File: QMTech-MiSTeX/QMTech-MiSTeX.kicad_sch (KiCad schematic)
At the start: 42 parts, among them J1 RPi_GPIO, J12 Conn_01x03_Pin, J13 USB_C_Receptacle_USB2.0, J2 MiSTer SDRAM Module, J3 USB_C_Receptacle_USB2.0, J4 Conn_02x32_Odd_Even, J5 Conn_02x32_Odd_Even, J6 Conn_01x06_Pin, J7 Conn_01x03_Pin, J8 Conn_01x03_Pin

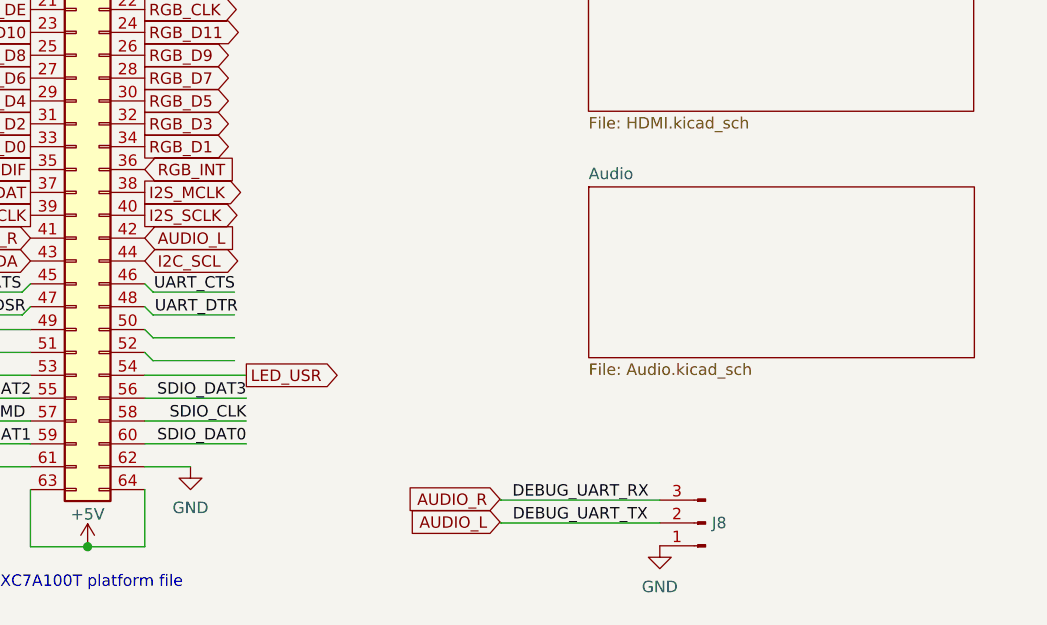
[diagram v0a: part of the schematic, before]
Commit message: connect two remaining pins to new 2 row Pmod, fix via, tidy test points
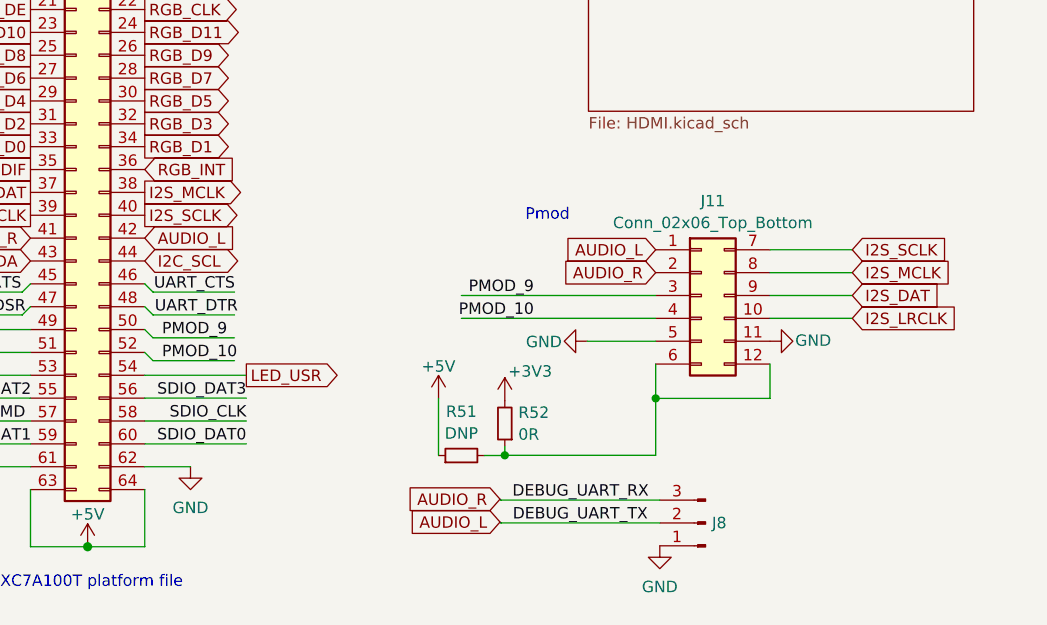
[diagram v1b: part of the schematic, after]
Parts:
- added J11: Conn_02x06_Top_Bottom, Connector_PinSocket_2.54mm:PinSocket_2x06_P2.54mm_Horizontal, symbol Connector_Generic:Conn_02x06_Top_Bottom
- added R51: DNP, R_0603_1608Metric, symbol jlcpcb-basic-resistor-0603:0R
- added R52: 0R, R_0603_1608Metric, symbol jlcpcb-basic-resistor-0603:0R
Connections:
- net +3V3: now also R52.2
- net +5V: now also R51.1
- net AUDIO_L: now also J11.1 (Pin_1)
- net AUDIO_R: now also J11.2 (Pin_2)
- net GND: now also J11.11 (Pin_11), J11.5 (Pin_5)
- net I2S_DAT: now also J11.9 (Pin_9)
- net I2S_LRCLK: now also J11.10 (Pin_10)
- net I2S_MCLK: now also J11.8 (Pin_8)
- net I2S_SCLK: now also J11.7 (Pin_7)
- net PMOD_9: now reaches J5.50 (Pin_50)
- net PMOD_9: now also J11.3 (Pin_3)
- net PMOD_10: now reaches J5.52 (Pin_52)
- net PMOD_10: now also J11.4 (Pin_4)
- new net: J11.12 (Pin_12), J11.6 (Pin_6), R51.2, R52.1
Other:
- removed sheet Audio
- note added: "Pmod"

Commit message: don't include DNP parts in BOM
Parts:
- R51: LCSC C21189 -> (none)
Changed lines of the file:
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@@
-      (effects (font (size 1.27 1.27)) hide)
-    )
-    (property "LCSC" "C21189" (at 217.17 93.98 90)
       (effects (font (size 1.27 1.27)) hide)
     )

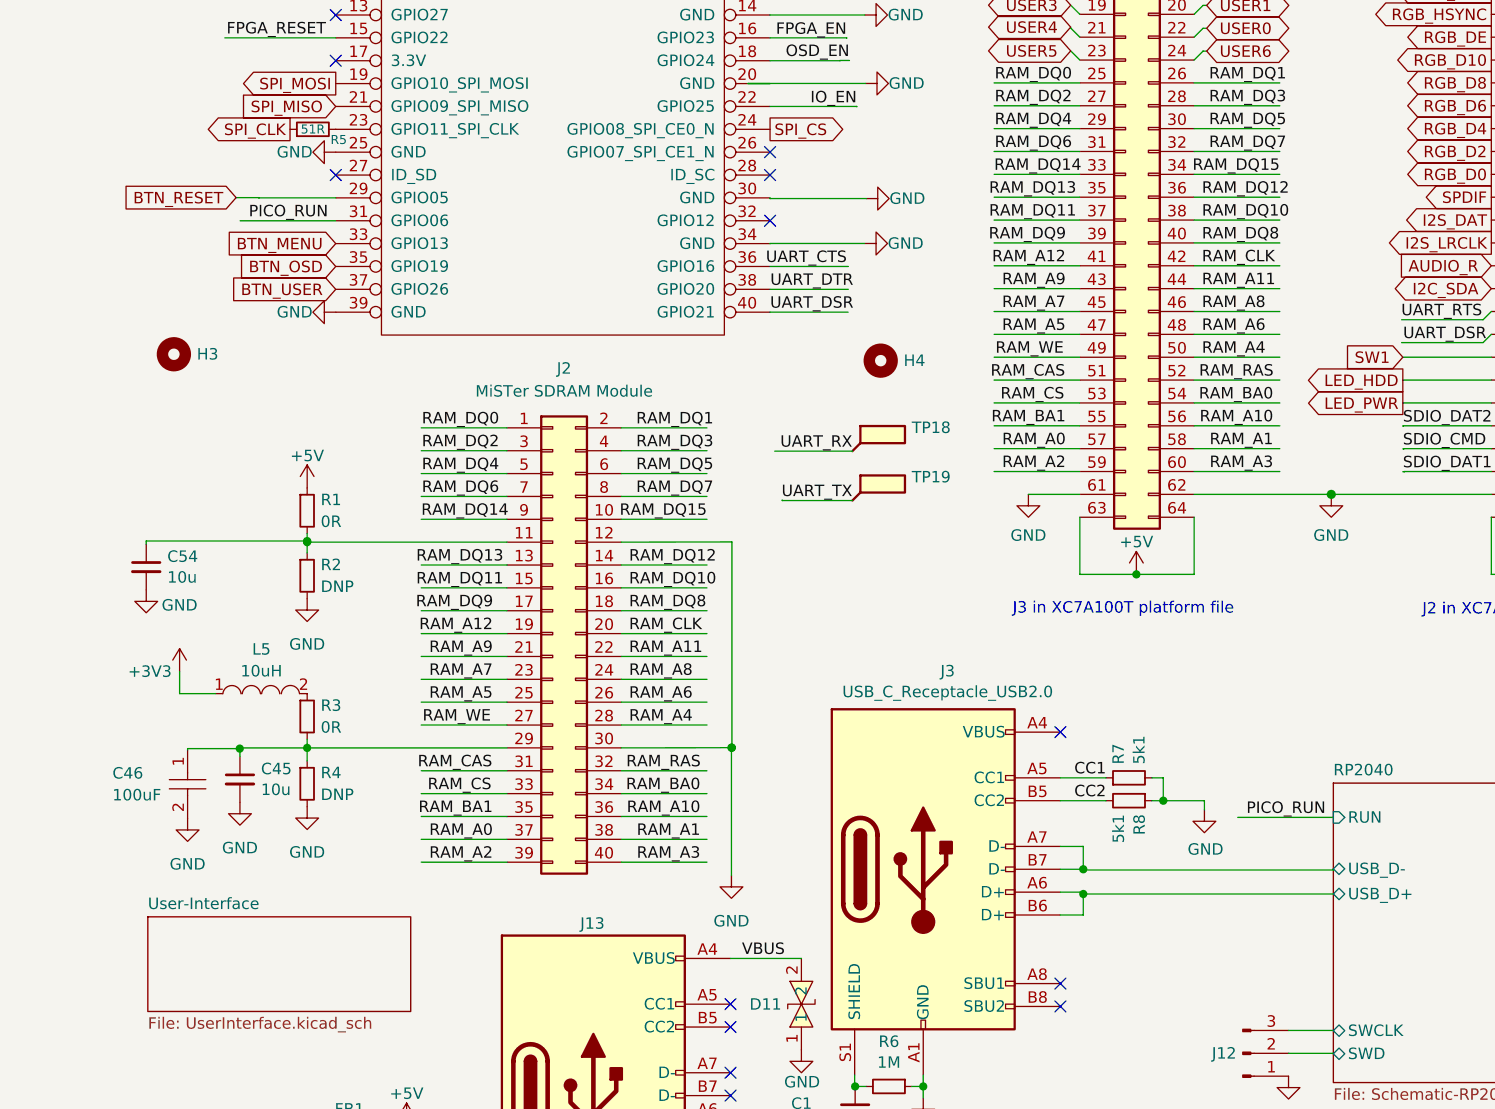
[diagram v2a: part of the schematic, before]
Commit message: add front switch, reroute USB, test points
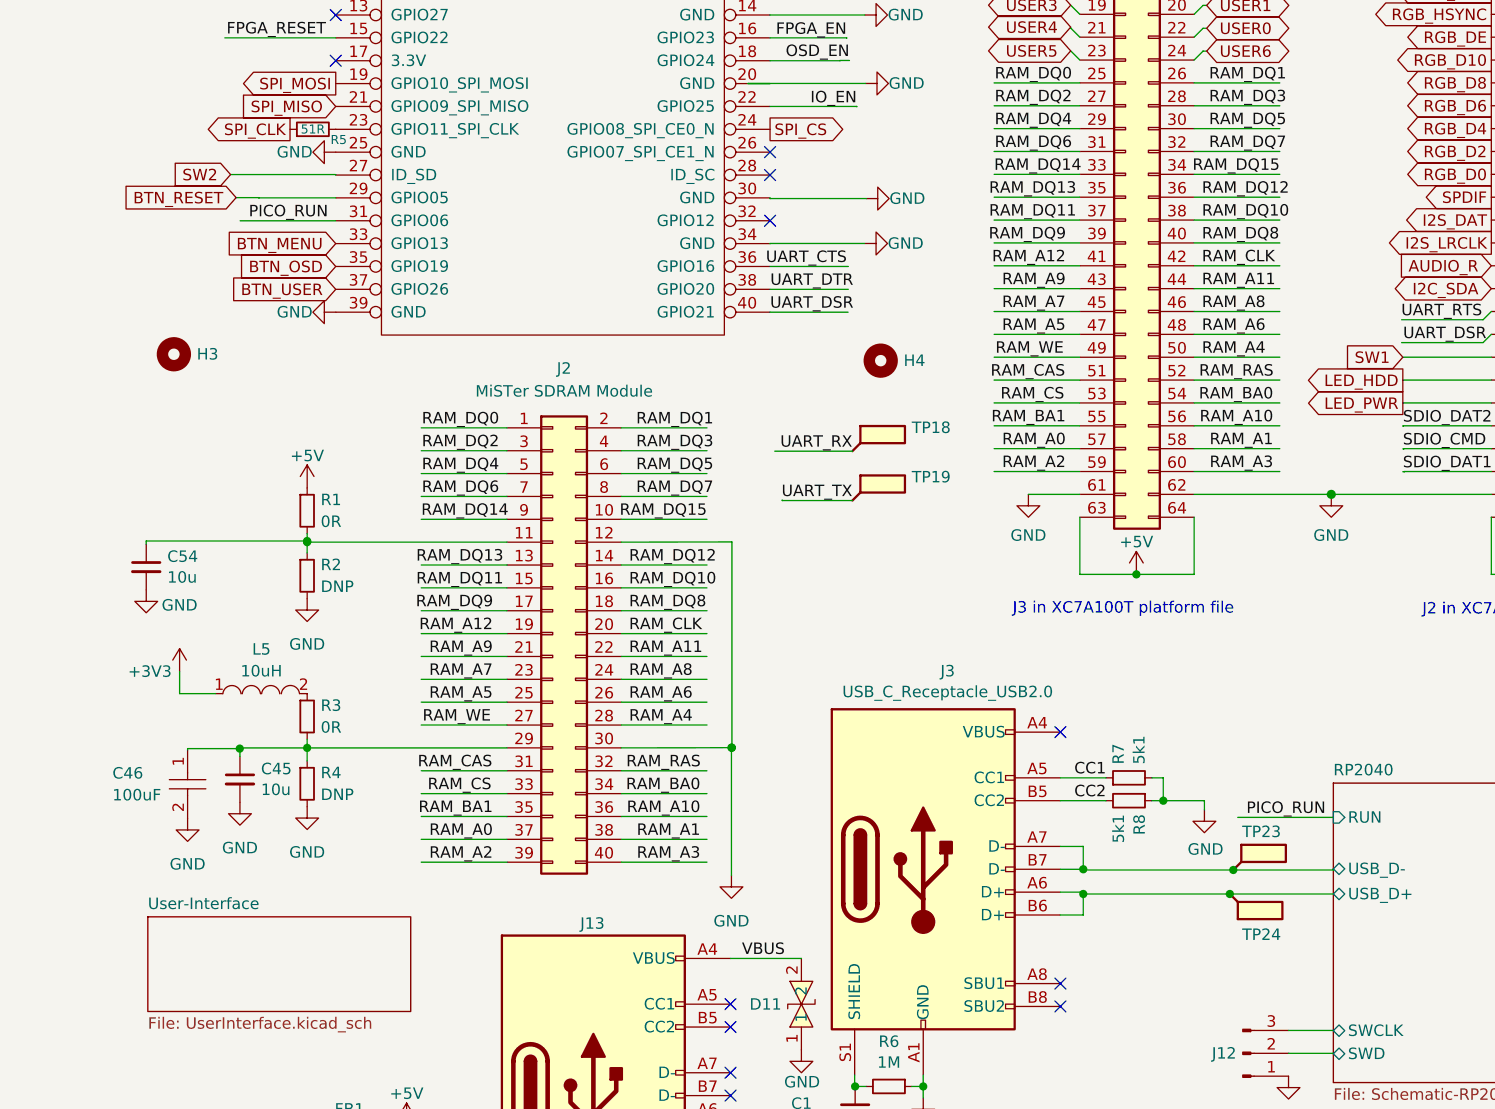
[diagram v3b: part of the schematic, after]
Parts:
- added TP23, TP24: TestPoint_Flag, TestPoint:TestPoint_Pad_D1.5mm, symbol Connector:TestPoint_Flag
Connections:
- net RP2040/USB_D+: now also TP24.1
- net RP2040/USB_D-: now also TP23.1
- net SW2: now reaches J1.27 (ID_SD)
- no-connect marks 20 -> 19
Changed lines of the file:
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@@
   (junction (at 84.9122 123.3678) (diameter 0) (color 0 0 0 0)
   )
+  (junction (at 140.2377 139.6238) (diameter 0) (color 0 0 0 0)
+  )
   (junction (at 175.641 104.1146) (diameter 1.016) (color 0 0 0 0)
   )
@@
   (junction (at 123.952 139.6238) (diameter 0) (color 0 0 0 0)
   )
+  (junction (at 140.6214 136.9568) (diameter 0) (color 0 0 0 0)
+  )
   (junction (at 238.76 87.63) (diameter 0) (color 0 0 0 0)
   )
@@
   (no_connect (at 40.894 26.7208))
   (no_connect (at 84.7598 177.2666))
-  (no_connect (at 40.894 59.7408))
   (no_connect (at 89.154 64.8208))
   (no_connect (at 89.154 59.7408))
@@
     (stroke (width 0) (type default))
   )
+  (wire (pts (xy 29.21 59.69) (xy 40.894 59.69))
+    (stroke (width 0) (type default))
+  )
   (wire (pts (xy 245.364 151.765) (xy 228.2952 151.765))
     (stroke (width 0) (type default))
@@
     (stroke (width 0) (type default))
   )
+  (wire (pts (xy 40.894 59.69) (xy 40.894 59.7408))
+    (stroke (width 0) (type default))
+  )
   (wire (pts (xy 182.9054 80.899) (xy 181.991 79.9846))
     (stroke (width 0) (type default))
@@
     (stroke (width 0) (type default))
   )
+  (wire (pts (xy 140.6214 136.9568) (xy 151.7396 136.9568))
+    (stroke (width 0) (type default))
+  )
   (wire (pts (xy 181.991 97.7646) (xy 181.991 104.1146))
     (stroke (width 0) (type solid))
@@
     (stroke (width 0) (type default))
   )
+  (wire (pts (xy 140.2377 139.6238) (xy 151.7396 139.6238))
+    (stroke (width 0) (type default))
+  )
   (wire (pts (xy 151.7142 154.7876) (xy 151.7396 154.813))
     (stroke (width 0) (type default))
@@
     (stroke (width 0) (type default))
   )
-  (wire (pts (xy 123.952 139.6238) (xy 151.7396 139.6238))
+  (wire (pts (xy 123.952 139.6238) (xy 140.2377 139.6238))
     (stroke (width 0) (type default))
   )
@@
     (stroke (width 0) (type default))
   )
-  (wire (pts (xy 123.952 136.9568) (xy 151.7396 136.9568))
+  (wire (pts (xy 123.952 136.9568) (xy 140.6214 136.9568))
     (stroke (width 0) (type default))
   )
@@
     )
   )
+  (global_label "SW2" (shape input) (at 29.21 59.69 180) (fields_autoplaced)
+    (effects (font (size 1.27 1.27)) (justify right))
+    (property "Intersheetrefs" "${INTERSHEET_REFS}" (at 22.2593 59.69 0)
+      (effects (font (size 1.27 1.27)) (justify right))
+    )
+  )
   (global_label "RGB_D12" (shape output) (at 169.291 39.3446 180) (fields_autoplaced)
     (effects (font (size 1.27 1.27)) (justify right))
@@
     )
   )
+  (symbol (lib_id "Connector:TestPoint_Flag") (at 140.2377 139.6238 0) (mirror x) (unit 1)
+    (in_bom yes) (on_board yes) (dnp no)
+    (property "Reference" "TP24" (at 141.605 144.145 0)
+      (effects (font (size 1.27 1.27)) (justify left))
+    )
+    (property "Value" "TestPoint_Flag" (at 146.8417 139.8087 0)
+      (effects (font (size 1.27 1.27)) (justify left) hide)
+    )
+    (property "Footprint" "TestPoint:TestPoint_Pad_D1.5mm" (at 145.3177 139.6238 0)
+      (effects (font (size 1.27 1.27)) hide)
+    )
+    (property "Datasheet" "~" (at 145.3177 139.6238 0)
+      (effects (font (size 1.27 1.27)) hide)
+    )
+    (pin "1")
+    (instances
+      (project "QMTech-MiSTeX"
+        (path "/bf95850e-2fcb-4784-a603-f17fc357556b"
+          (reference "TP24") (unit 1)
+        )
+      )
+    )
+  )
   (symbol (lib_id "Connector:TestPoint_Flag") (at 98.298 90.424 0) (unit 1)
     (in_bom yes) (on_board yes) (dnp no) (fields_autoplaced)
@@
         )
       )
+    )
+  )
+  (symbol (lib_id "Connector:TestPoint_Flag") (at 140.6214 136.9568 0) (unit 1)
+    (in_bom yes) (on_board yes) (dnp no)
+    (property "Reference" "TP23" (at 141.605 132.715 0)
+      (effects (font (size 1.27 1.27)) (justify left))
+    )
+    (property "Value" "TestPoint_Flag" (at 147.2254 136.7719 0)
+      (effects (font (size 1.27 1.27)) (justify left) hide)
+    )
+    (property "Footprint" "TestPoint:TestPoint_Pad_D1.5mm" (at 145.7014 136.9568 0)
+      (effects (font (size 1.27 1.27)) hide)
+    )
+    (property "Datasheet" "~" (at 145.7014 136.9568 0)
+      (effects (font (size 1.27 1.27)) hide)
+    )
+    (pin "1")
+    (instances
+      (project "QMTech-MiSTeX"
+        (path "/bf95850e-2fcb-4784-a603-f17fc357556b"
+          (reference "TP23") (unit 1)
+        )
+      )

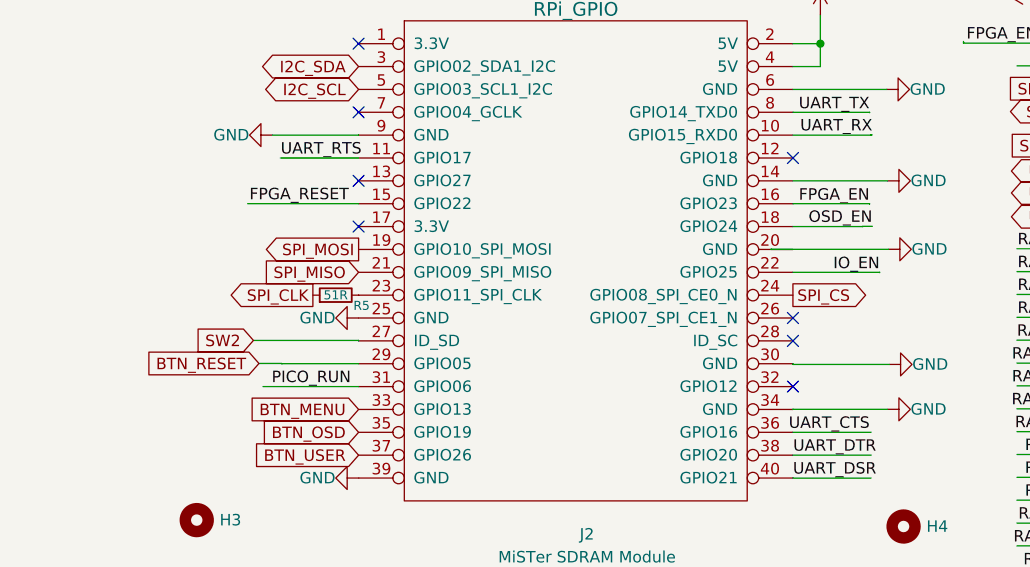
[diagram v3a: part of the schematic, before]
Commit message: Add VGA green probe, add DIP switches, add to silk screen, cosmetics
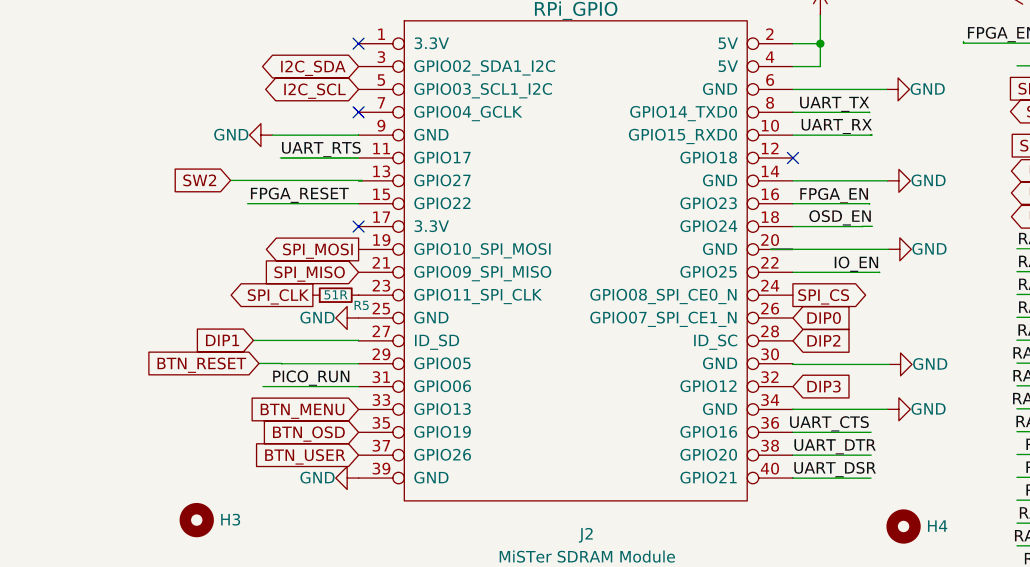
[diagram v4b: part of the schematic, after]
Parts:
- R2: LCSC C17477 -> (none)
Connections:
- net SW2: now also J1.13 (GPIO27); no longer J1.27 (ID_SD)
- net DIP0: now reaches J1.26 (GPIO07_SPI_CE1_N)
- net DIP2: now reaches J1.28 (ID_SC)
- net DIP3: now reaches J1.32 (GPIO12)
- new net DIP1: J1.27 (ID_SD)
- no-connect marks 19 -> 15
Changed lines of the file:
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@@
   (no_connect (at 84.7598 174.7266))
   (no_connect (at 40.894 34.3408))
-  (no_connect (at 89.154 57.2008))
-  (no_connect (at 40.894 41.9608))
+  (no_connect (at 40.894 47.0408))
   (no_connect (at 121.412 152.1206))
   (no_connect (at 84.7598 154.4066))
@@
   (no_connect (at 40.894 26.7208))
   (no_connect (at 84.7598 177.2666))
-  (no_connect (at 89.154 64.8208))
-  (no_connect (at 89.154 59.7408))
   (no_connect (at 89.154 39.4208))
-  (no_connect (at 40.894 47.0408))
   (no_connect (at 84.7598 159.4866))
   (no_connect (at 84.7598 167.1066))
@@
     (stroke (width 0) (type default))
   )
+  (wire (pts (xy 26.67 41.91) (xy 41.275 41.91))
+    (stroke (width 0) (type default))
+  )
   (wire (pts (xy 182.9054 75.819) (xy 181.991 74.9046))
     (stroke (width 0) (type default))
@@
     (stroke (width 0) (type solid))
   )
+  (wire (pts (xy 41.275 41.91) (xy 41.275 41.9608))
+    (stroke (width 0) (type default))
+  )
   (wire (pts (xy 27.559 117.3619) (xy 23.5458 117.3619))
     (stroke (width 0) (type default))
@@
     (stroke (width 0) (type default))
   )
+  (wire (pts (xy 41.275 41.9608) (xy 40.894 41.9608))
+    (stroke (width 0) (type default))
+  )
   (wire (pts (xy 48.768 165.4048) (xy 48.768 166.6748))
     (stroke (width 0) (type default))
@@
     )
   )
+  (global_label "DIP2" (shape input) (at 89.154 59.7408 0) (fields_autoplaced)
+    (effects (font (size 1.27 1.27)) (justify left))
+    (property "Intersheetrefs" "${INTERSHEET_REFS}" (at 96.5886 59.7408 0)
+      (effects (font (size 1.27 1.27)) (justify left))
+    )
+  )
   (global_label "LED_HDD" (shape output) (at 159.4612 82.55 180) (fields_autoplaced)
     (effects (font (size 1.27 1.27)) (justify right))
@@
     )
   )
-  (global_label "SW2" (shape input) (at 29.21 59.69 180) (fields_autoplaced)
+  (global_label "DIP3" (shape input) (at 89.154 64.8208 0) (fields_autoplaced)
+    (effects (font (size 1.27 1.27)) (justify left))
+    (property "Intersheetrefs" "${INTERSHEET_REFS}" (at 96.5886 64.8208 0)
+      (effects (font (size 1.27 1.27)) (justify left))
+    )
+  )
+  (global_label "SW2" (shape input) (at 26.67 41.91 180) (fields_autoplaced)
     (effects (font (size 1.27 1.27)) (justify right))
-    (property "Intersheetrefs" "${INTERSHEET_REFS}" (at 22.2593 59.69 0)
+    (property "Intersheetrefs" "${INTERSHEET_REFS}" (at 19.7193 41.91 0)
       (effects (font (size 1.27 1.27)) (justify right))
     )
@@
     )
   )
+  (global_label "DIP1" (shape input) (at 29.21 59.69 180) (fields_autoplaced)
+    (effects (font (size 1.27 1.27)) (justify right))
+    (property "Intersheetrefs" "${INTERSHEET_REFS}" (at 21.7754 59.69 0)
+      (effects (font (size 1.27 1.27)) (justify right))
+    )
+  )
   (global_label "I2S_DAT" (shape output) (at 169.291 64.7446 180) (fields_autoplaced)
     (effects (font (size 1.27 1.27)) (justify right))
@@
     )
   )
+  (global_label "DIP0" (shape input) (at 89.154 57.2008 0) (fields_autoplaced)
+    (effects (font (size 1.27 1.27)) (justify left))
+    (property "Intersheetrefs" "${INTERSHEET_REFS}" (at 96.5886 57.2008 0)
+      (effects (font (size 1.27 1.27)) (justify left))
+    )
+  )
   (global_label "I2C_SCL" (shape bidirectional) (at 181.991 72.3646 0) (fields_autoplaced)
     (effects (font (size 1.27 1.27)) (justify left))
@@
       (effects (font (size 1.27 1.27)) hide)
     )
-    (property "LCSC" "C17477" (at 37.719 104.267 90)
-      (effects (font (size 1.27 1.27)) hide)
-    )
